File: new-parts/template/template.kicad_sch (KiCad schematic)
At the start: 4 parts, among them J1 BHR-10-VUA, J2 BHR-10-VUA, K1 J104D2C12VDC.15S

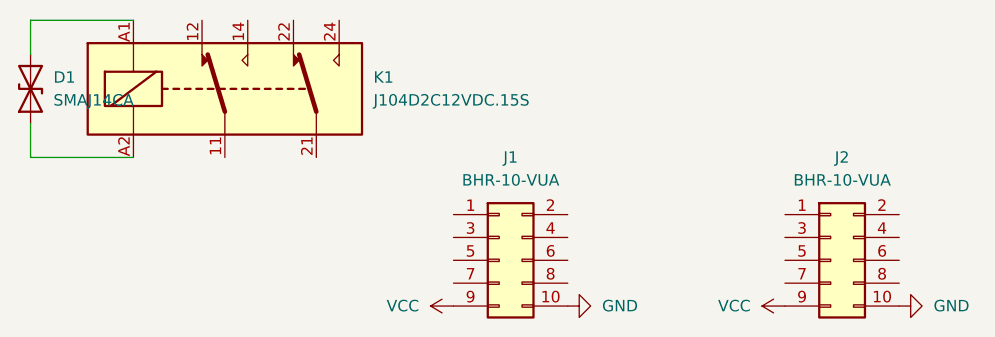
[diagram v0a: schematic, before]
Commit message: template: import design rules.
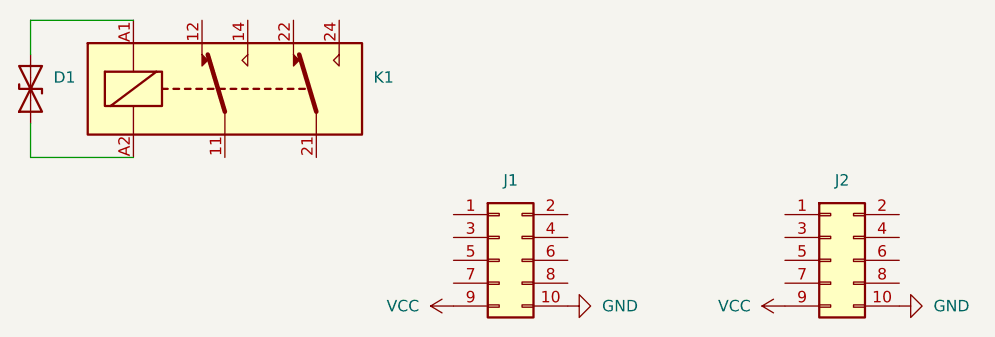
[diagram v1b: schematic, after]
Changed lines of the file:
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@@
   )
   (symbol (lib_id "Connector_Generic:Conn_02x05_Odd_Even") (at 111.76 50.8 0) (unit 1)
-    (in_bom yes) (on_board yes) (dnp no) (fields_autoplaced)
-    (property "Reference" "J2" (at 113.03 39.37 0)
+    (in_bom yes) (on_board yes) (dnp no)
+    (property "Reference" "J2" (at 113.03 41.91 0)
       (effects (font (size 1.27 1.27)))
     )
     (property "Value" "BHR-10-VUA" (at 113.03 41.91 0)
-      (effects (font (size 1.27 1.27)))
+      (effects (font (size 1.27 1.27)) hide)
     )
     (property "Footprint" "Connector_IDC:IDC-Header_2x05_P2.54mm_Vertical" (at 111.76 50.8 0)
@@
   )
   (symbol (lib_id "Connector_Generic:Conn_02x05_Odd_Even") (at 74.93 50.8 0) (unit 1)
-    (in_bom yes) (on_board yes) (dnp no) (fields_autoplaced)
-    (property "Reference" "J1" (at 76.2 39.37 0)
+    (in_bom yes) (on_board yes) (dnp no)
+    (property "Reference" "J1" (at 76.2 41.91 0)
       (effects (font (size 1.27 1.27)))
     )
     (property "Value" "BHR-10-VUA" (at 76.2 41.91 0)
-      (effects (font (size 1.27 1.27)))
+      (effects (font (size 1.27 1.27)) hide)
     )
     (property "Footprint" "Connector_IDC:IDC-Header_2x05_P2.54mm_Vertical" (at 74.93 50.8 0)
@@
     )
     (property "Value" "J104D2C12VDC.15S" (at 60.96 33.02 0)
-      (effects (font (size 1.27 1.27)) (justify left))
+      (effects (font (size 1.27 1.27)) (justify left) hide)
     )
     (property "Footprint" "Relay_THT:Relay_DPDT_Finder_30.22" (at 60.96 33.02 0)
@@
     )
     (property "Value" "SMAJ14CA" (at 25.4 33.02 90)
-      (effects (font (size 1.27 1.27)) (justify right))
+      (effects (font (size 1.27 1.27)) (justify right) hide)
     )
     (property "Footprint" "Diode_SMD:D_SMA_Handsoldering" (at 22.86 31.75 0)
